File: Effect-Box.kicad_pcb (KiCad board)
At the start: 6 copper layers, 170 parts, among them J1 Conn_02x07_Odd_Even, J10 Power pins, J2 26642801RP2, J3 FH12A-10S-0.5SH55, J5 Conn_ARM_JTAG_SWD_20, J6 26642801RP2, J7 AudioJack3, J8 AudioJack3, J9 PJ-006A-SMT, SW0 SW_Push, SW1 SW_Push, SW2 SW_Push, SW3 SW_Push, SW4 SW_Push, SW5 SW_Push, SW6 SW_Push, U1 TPS54325, U10 LM7805SX_NOPB, U2 TPS54294, U3 XC7A100T-FTG256, U4 S25FL1, U5 SiT2024B, U6 AS6C1616, U7 EFM32GG942F1024, U8 INA1651IPW, U9 PCM3003E

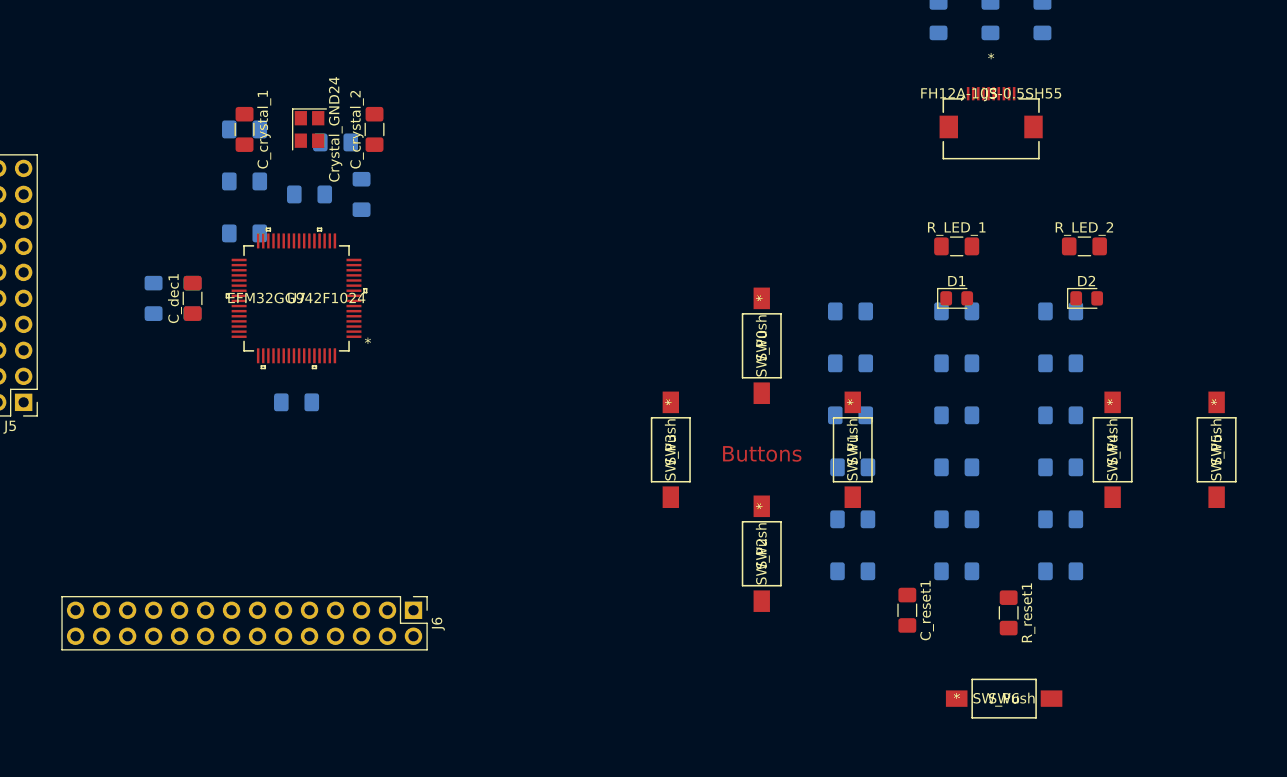
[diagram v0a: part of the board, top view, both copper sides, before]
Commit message: Partially route MCU
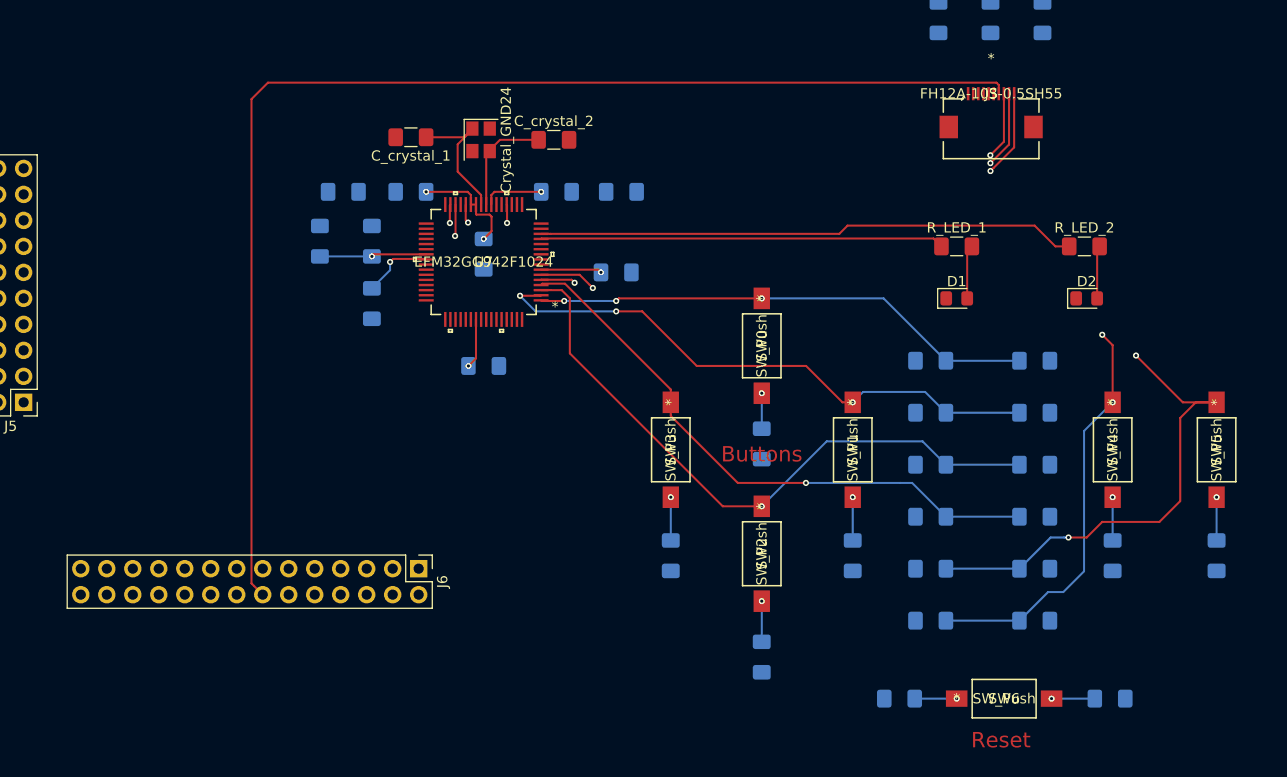
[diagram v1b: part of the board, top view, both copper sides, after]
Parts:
- C_dec1, C_reset1, R_reset1: moved to B.Cu
- moved C_iovdd_0 38.9 mm to (136.7, 116.8)
- moved R_btn_4 35.6 mm to (195.3, 144.5), turned to 90 degrees
- moved C_avdd1 28.4 mm to (137.2, 109.0)
- moved R_btn_3 25.7 mm to (142.0, 144.5), turned to 90 degrees
- moved R_btn_5 25.6 mm to (185.2, 144.5), turned to 90 degrees
- moved C_iovdd_3 23.5 mm to (123.7, 115.1), turned to 270 degrees
- moved R_btn_2 20.6 mm to (150.9, 154.4), turned to 90 degrees
- moved C_avdd_1 19.1 mm to (130.8, 109.0), turned to 0 degrees
- moved C_iovdd_5 18.6 mm to (123.7, 126.0)
- moved U7 18.6 mm to (123.7, 115.8)
- moved C_vdd_1 18.4 mm to (112.8, 113.8)
- moved C_crystal_2 17.6 mm to (130.6, 103.9), turned to 0 degrees
- moved C_dec1 17.5 mm to (112.8, 119.9), turned to 270 degrees
- moved C_vdd1 17.2 mm to (107.7, 113.8)
- moved Crystal_GND24 16.8 mm to (123.4, 103.9)
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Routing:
- net Net-(J3-Pad7): track 0.00 -> 123.5 mm
- net Net-(C_btn_4-Pad1): track 0.00 -> 108.9 mm, vias 0 -> 3
- net Net-(C_btn_5-Pad1): track 0.00 -> 97.5 mm, vias 0 -> 3
- net Net-(C_reset1-Pad1): track 0.00 -> 88.0 mm, vias 0 -> 2
- net Net-(J3-Pad10): track 0.00 -> 66.6 mm, vias 0 -> 2
- net Net-(J3-Pad8): track 0.00 -> 64.1 mm, vias 0 -> 2
- net Net-(J3-Pad9): track 0.00 -> 63.0 mm, vias 0 -> 2
- net Net-(C_btn_2-Pad1): track 0.00 -> 62.2 mm, vias 0 -> 1
- net Net-(C_btn_3-Pad1): track 0.00 -> 57.7 mm, vias 0 -> 1
- net Net-(C_btn_1-Pad1): track 0.00 -> 56.5 mm, vias 0 -> 3
- net Net-(R_LED_2-Pad1): track 0.00 -> 52.8 mm
- net Net-(C_btn_0-Pad1): track 0.00 -> 49.4 mm, vias 0 -> 3
- net Net-(R_LED_1-Pad1): track 0.00 -> 39.5 mm
- net +3V3: track 4.67 -> 42.9 mm, vias 13 -> 19
- net Net-(C_crystal_1-Pad1): track 0.00 -> 13.8 mm
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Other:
- board text added: "Reset"

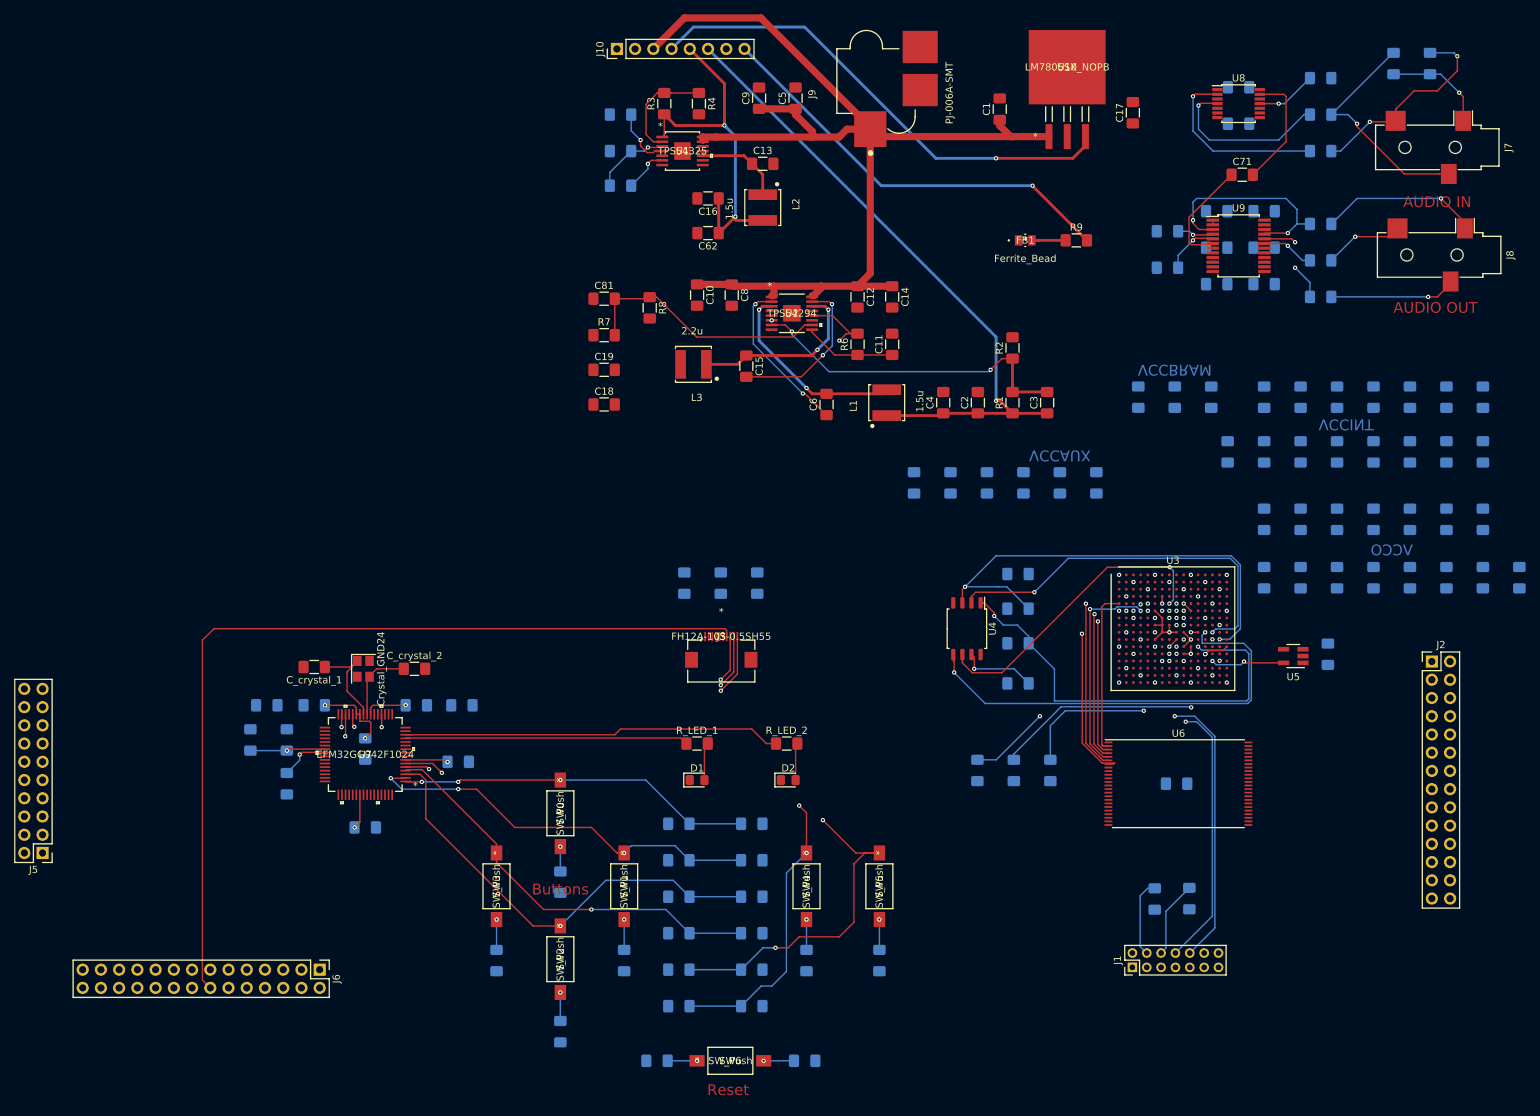
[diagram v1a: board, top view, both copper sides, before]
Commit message: Route MCU header
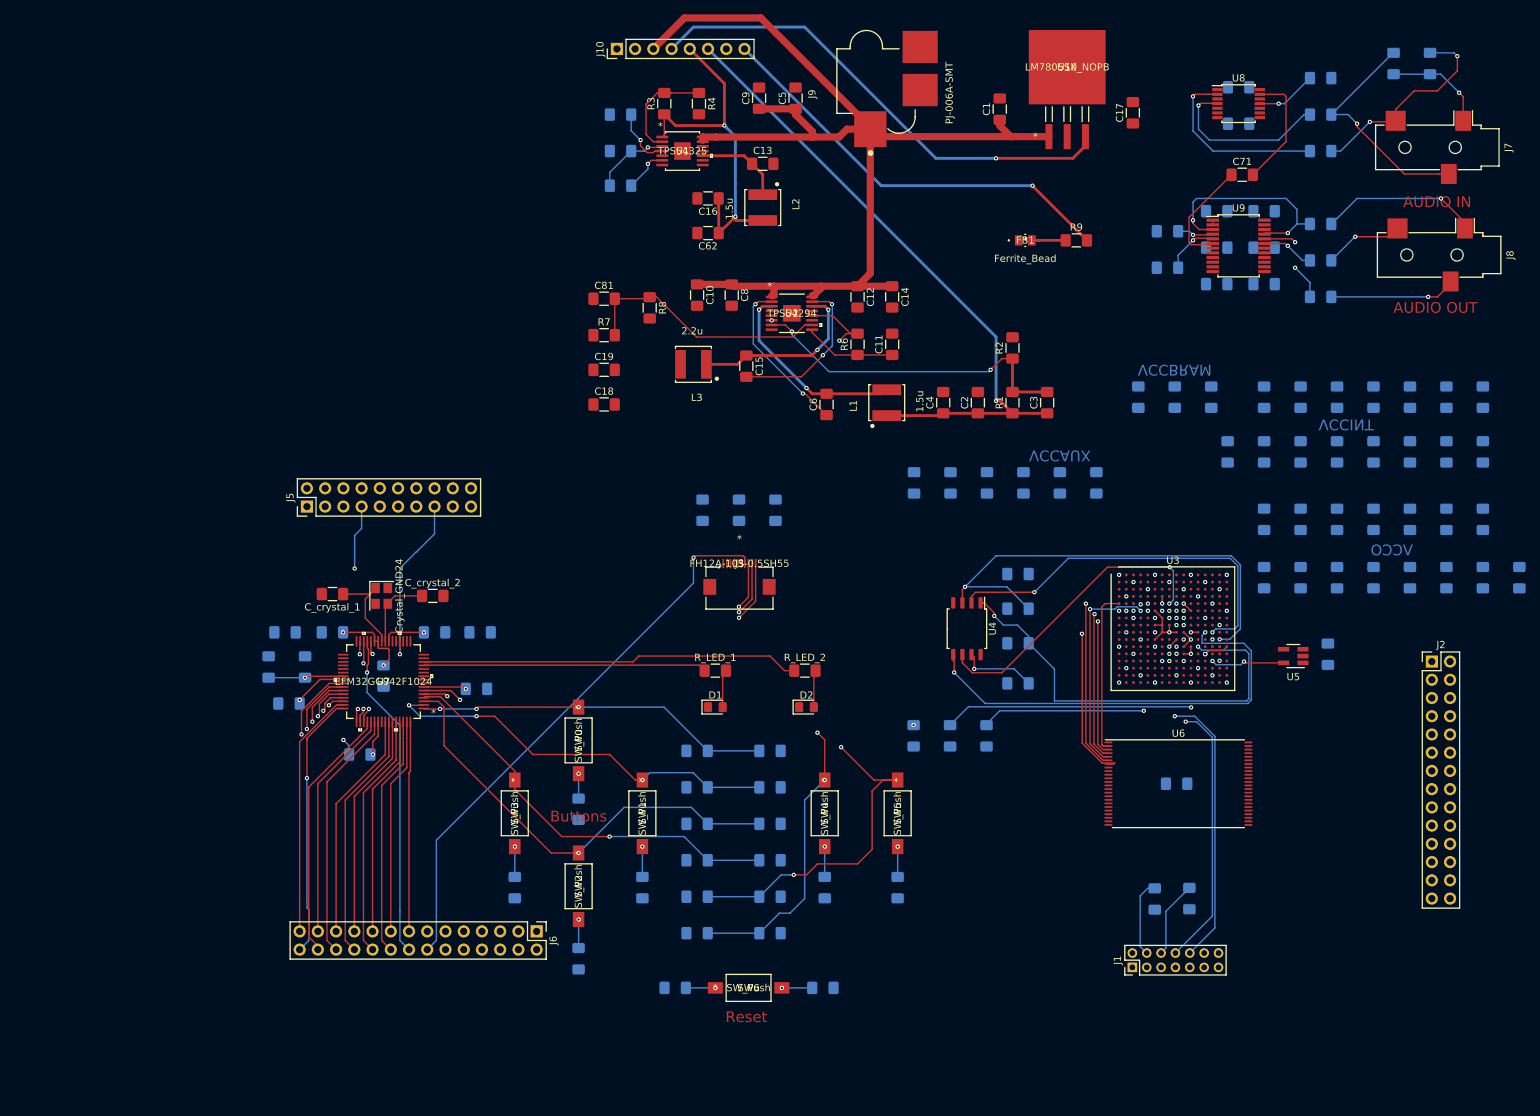
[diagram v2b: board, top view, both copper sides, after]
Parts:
- moved J5 60.7 mm to (115.6, 81.3), turned to 90 degrees
- moved J6 30.7 mm to (147.6, 140.5)
- moved C_dec1 11.2 mm to (113.1, 108.7), turned to 180 degrees
- moved R_btn_up_1 10.5 mm to (180.1, 120.4)
- moved C_crystal_1 10.5 mm to (119.1, 93.5)
- moved C_btn_1 10.5 mm to (169.9, 120.4)
- moved R_btn_0 10.5 mm to (153.4, 123.4)
- moved C_iovdd_0 10.5 mm to (139.2, 106.7)
- moved D1 10.5 mm to (172.5, 109.2)
- moved R_LED_1 10.5 mm to (172.5, 104.1)
- moved R_btn_1 10.5 mm to (162.3, 134.4)
- moved R_btn_3 10.5 mm to (144.5, 134.4)
- moved R_btn_4 10.5 mm to (197.9, 134.4)
- moved R_btn_up_0 10.5 mm to (180.1, 115.3)
- moved R_btn_up_2 10.5 mm to (180.1, 125.5)
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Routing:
- net Net-(J6-Pad8): track 0.00 -> 51.1 mm, vias 0 -> 1
- net Net-(J6-Pad6): track 0.00 -> 49.9 mm, vias 0 -> 1
- net Net-(J6-Pad4): track 0.00 -> 48.5 mm, vias 0 -> 1
- net Net-(J6-Pad7): track 0.00 -> 47.4 mm, vias 0 -> 1
- net Net-(J6-Pad5): track 0.00 -> 46.2 mm, vias 0 -> 1
- net Net-(J6-Pad16): track 0.00 -> 45.5 mm, vias 0 -> 1
- net Net-(J3-Pad7): track 123.5 -> 78.2 mm, vias 0 -> 1
- net Net-(J6-Pad3): track 0.00 -> 44.7 mm, vias 0 -> 1
- net Net-(J6-Pad28): track 0.00 -> 36.9 mm, vias 0 -> 1
- net Net-(J6-Pad26): track 0.00 -> 35.6 mm
- net Net-(J6-Pad24): track 0.00 -> 35.0 mm
- net Net-(J6-Pad22): track 0.00 -> 34.8 mm
- net Net-(J5-Pad13): track 0.00 -> 34.6 mm, vias 0 -> 1
- net Net-(J6-Pad27): track 0.00 -> 34.6 mm
- net Net-(J6-Pad20): track 0.00 -> 34.1 mm
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
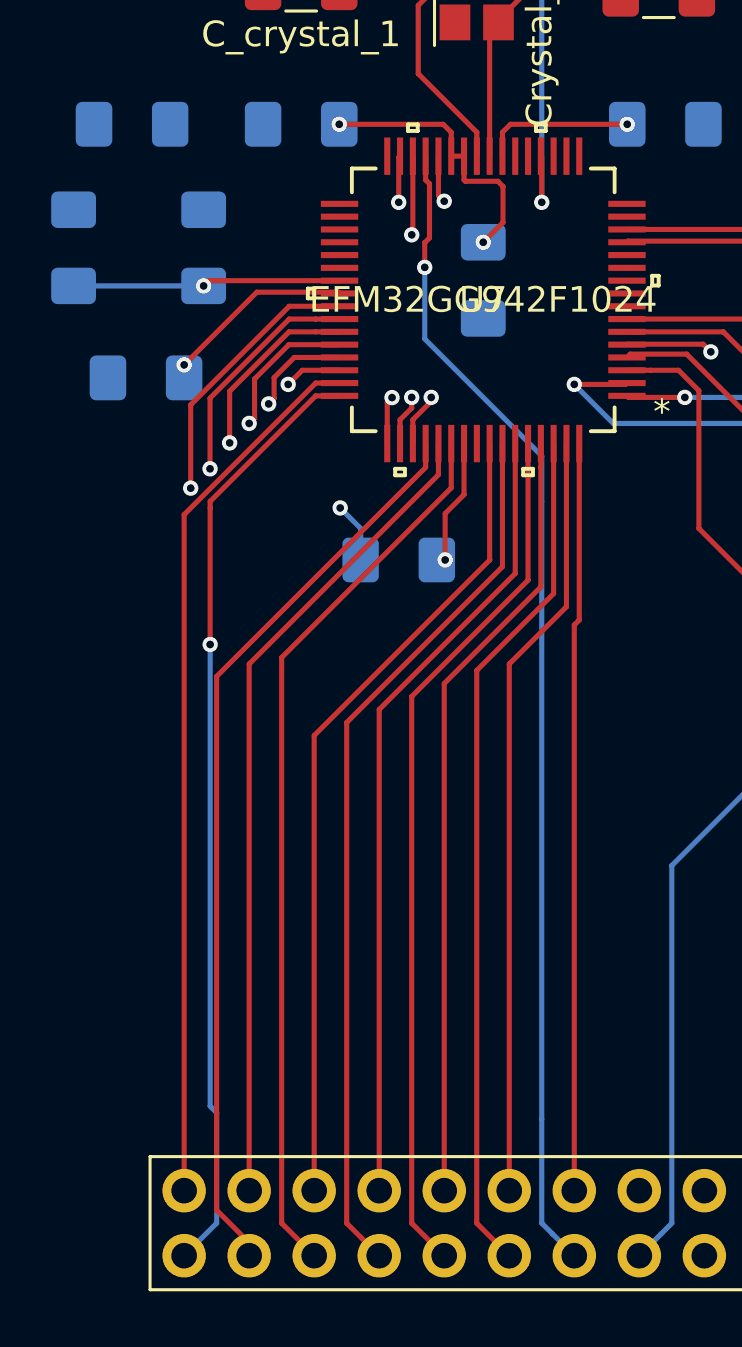
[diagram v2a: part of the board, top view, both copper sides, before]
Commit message: Route rest of MCU header
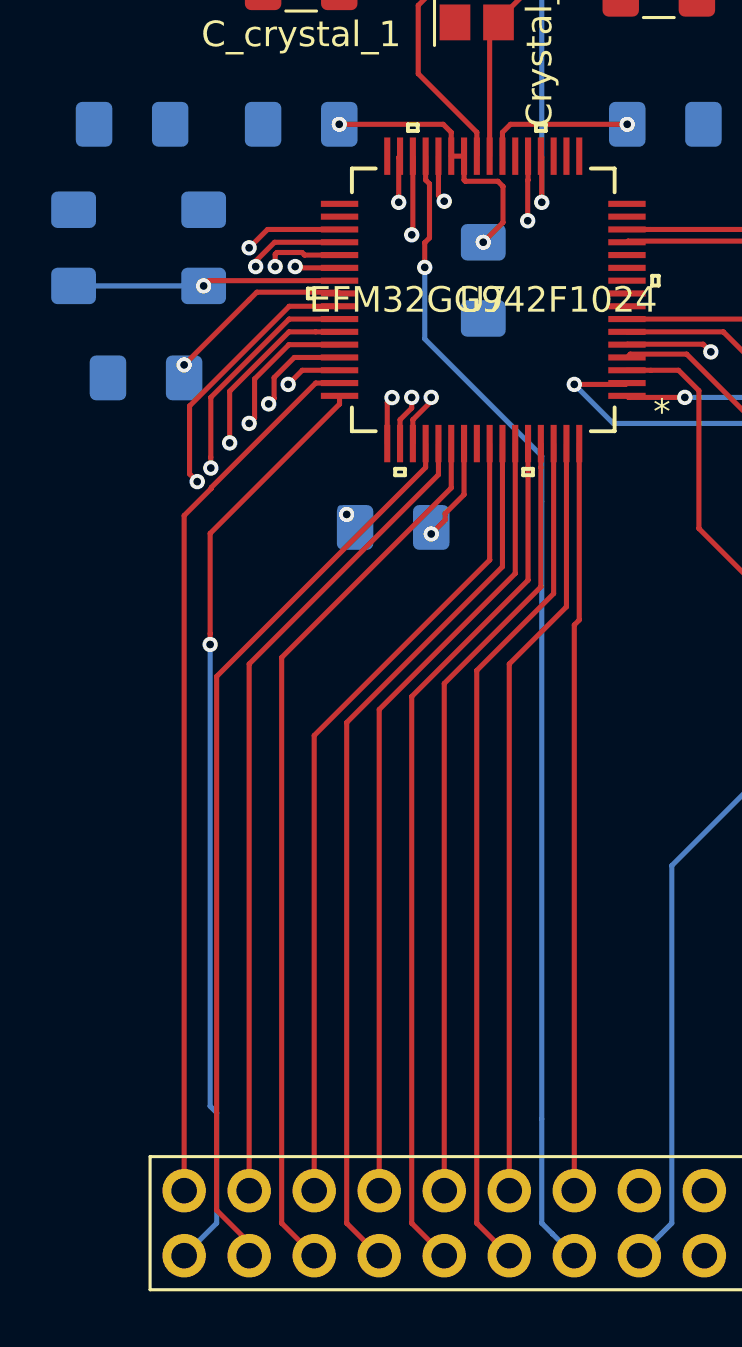
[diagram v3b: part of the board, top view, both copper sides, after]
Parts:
- moved C_iovdd_5 1.29 mm to (122.7, 114.6)
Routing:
- net Net-(J6-Pad12): track 0.00 -> 53.8 mm, vias 0 -> 1
- net Net-(J6-Pad10): track 0.00 -> 53.2 mm, vias 0 -> 1
- net Net-(J6-Pad11): track 0.00 -> 50.3 mm, vias 0 -> 1
- net Net-(J6-Pad9): track 0.00 -> 49.4 mm, vias 0 -> 1
- net Net-(J6-Pad13): track 0.00 -> 42.5 mm, vias 0 -> 1
- net GND: track 36.5 -> 35.3 mm
- net +3V3: track 42.9 -> 42.1 mm
- net Net-(J6-Pad28): track 36.9 -> 36.3 mm
